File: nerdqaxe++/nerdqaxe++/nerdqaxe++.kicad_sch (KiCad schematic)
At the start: 4 parts, among them J1 5.5mm/8A

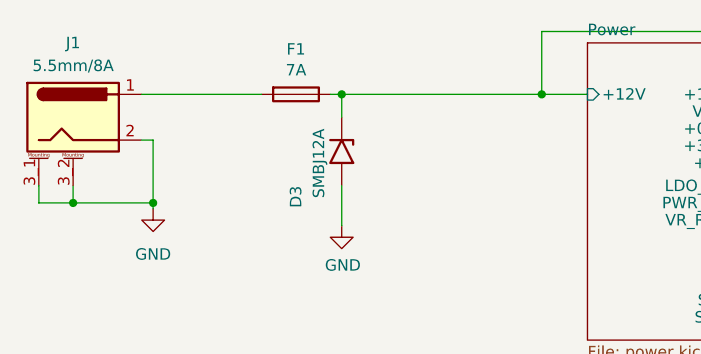
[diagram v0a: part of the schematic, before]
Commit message: updated fuse to 8A
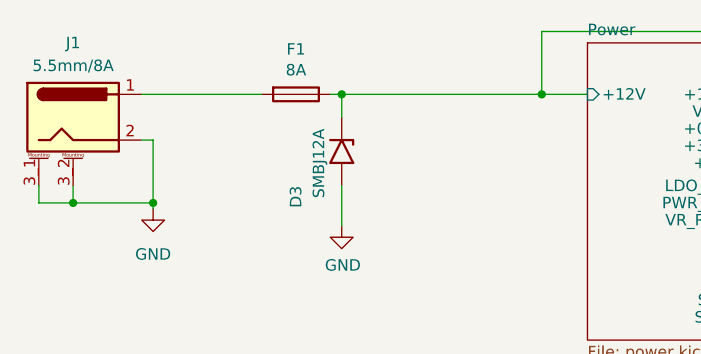
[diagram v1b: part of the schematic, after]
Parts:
- F1: value 7A -> 8A; Manufacturer 0154007.DR -> 0154008.DR; OrderNr F1229CT-ND -> F1239CT-ND
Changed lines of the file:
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@@
 			)
 		)
-		(property "Value" "7A"
+		(property "Value" "8A"
 			(at 50.165 49.3776 90)
 			(effects
@@
 			)
 		)
-		(property "Manufacturer" "0154007.DR"
+		(property "Manufacturer" "0154008.DR"
 			(at 50.165 52.07 0)
 			(effects
@@
 			)
 		)
-		(property "OrderNr" "F1229CT-ND"
+		(property "OrderNr" "F1239CT-ND"
 			(at 50.165 52.07 0)
 			(effects

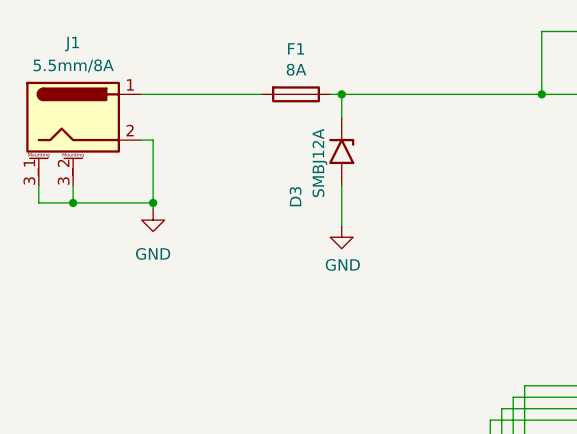
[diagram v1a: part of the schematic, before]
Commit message: removed solderjumpers on ++
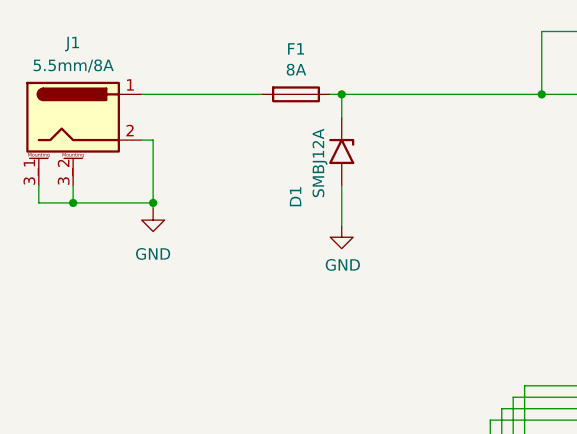
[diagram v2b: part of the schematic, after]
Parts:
- renumbered D3 to D1
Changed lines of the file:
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@@
 (kicad_sch
-	(version 20231120)
+	(version 20250114)
 	(generator "eeschema")
-	(generator_version "8.0")
+	(generator_version "9.0")
 	(paper "A")
 	(title_block
@@
 		(on_board yes)
 		(dnp no)
-		(property "Reference" "#PWR012"
+		(property "Reference" "#PWR04"
 			(at 55.245 73.025 0)
 			(effects
@@
 		(on_board yes)
 		(dnp no)
-		(property "Reference" "D3"
+		(property "Reference" "D1"
 			(at 50.165 62.23 0)
 			(effects
@@
 		(at 82.55 91.44)
 		(size 17.78 26.67)
+		(exclude_from_sim no)
+		(in_bom yes)
+		(on_board yes)
+		(dnp no)
 		(fields_autoplaced yes)
 		(stroke
@@
 		(at 82.55 46.355)
 		(size 17.145 33.02)
+		(exclude_from_sim no)
+		(in_bom yes)
+		(on_board yes)
+		(dnp no)
 		(fields_autoplaced yes)
 		(stroke
@@
 		(at 144.78 83.82)
 		(size 39.37 29.845)
+		(exclude_from_sim no)
+		(in_bom yes)
+		(on_board yes)
+		(dnp no)
 		(fields_autoplaced yes)
 		(stroke
@@
 		)
 	)
+	(embedded_fonts no)
 )
